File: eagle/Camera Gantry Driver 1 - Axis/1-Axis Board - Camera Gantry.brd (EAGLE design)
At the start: 73.3 x 46.5 mm, 48 parts, among them IC1 DRV8312A, U1 PTN78000, U2 DSPIC33FJ802GP-28, U3 LP2950-3.3ACZ

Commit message: Updating libraries and DRV83x2 related boards.
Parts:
- removed R6, R8, R9: (no value), pavlo:SMT-REF
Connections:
- removed net N$11: IC1.30, R8.1
- removed net N$12: IC1.38, R9.1
- removed net N$9: IC1.29, R6.1
- new net GND_A: IC1.29
- new net GND_B: IC1.30
- new net GND_C: IC1.38
- net GND: no longer R6.2, R8.2, R9.2
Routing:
- net N$12: track 21.8 -> 0.00 mm, vias 1 -> 0
- net N$9: track 10.4 -> 0.00 mm, vias 1 -> 0
- net N$11: track 9.39 -> 0.00 mm, vias 1 -> 0
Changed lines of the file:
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@@
 <?xml version="1.0" encoding="utf-8"?>
 <!DOCTYPE eagle SYSTEM "eagle.dtd">
-<eagle version="6.2">
+<eagle version="6.5.0">
 <drawing>
 <settings>
@@
 </class>
 </classes>
-<designrules>
+<designrules name="default">
 <description language="de">&lt;b&gt;EAGLE Design Rules&lt;/b&gt;
 &lt;p&gt;
@@
 <element name="E$3" library="ASL" package="STAND-OFF-TIGHT" value="" x="62.4" y="4"/>
 <element name="E$4" library="ASL" package="STAND-OFF-TIGHT" value="" x="11" y="4"/>
-<element name="R6" library="pavlo" package="SMT-REF" value="" x="18.364" y="30.75" rot="MR0"/>
-<element name="R8" library="pavlo" package="SMT-REF" value="" x="18.12" y="21.17" rot="MR90"/>
-<element name="R9" library="pavlo" package="SMT-REF" value="" x="26.38" y="14" rot="MR0"/>
 <element name="C18" library="ASL" package="CPOL-RADIAL-1000UF-25V" value="1000uF" x="23.622" y="35.96" rot="R270"/>
 <element name="C19" library="ASL" package="1206" value="10nF" x="21.082" y="42.672"/>
@@
 <wire x1="68.993" y1="11.23" x2="68.77" y2="11.23" width="0.4064" layer="1"/>
 <wire x1="68.77" y1="11.23" x2="67" y2="13" width="0.4064" layer="1"/>
-<contactref element="R6" pad="2"/>
-<contactref element="R8" pad="2"/>
-<contactref element="R9" pad="2"/>
 <contactref element="C19" pad="2"/>
 <contactref element="C18" pad="2"/>
@@
 <wire x1="31.5425" y1="22.8525" x2="32.25" y2="23.56" width="0.4064" layer="1"/>
 </signal>
-<signal name="N$9">
-<contactref element="IC1" pad="29"/>
-<contactref element="R6" pad="1"/>
-<wire x1="19.35" y1="26.0275" x2="17.4065" y2="26.0275" width="0.4064" layer="1"/>
-<wire x1="17.4065" y1="26.0275" x2="16.002" y2="27.432" width="0.4064" layer="1"/>
-<wire x1="16.002" y1="27.432" x2="14.986" y2="27.432" width="0.4064" layer="1"/>
-<wire x1="14.986" y1="27.432" x2="14.732" y2="27.178" width="0.4064" layer="1"/>
-<via x="14.732" y="27.178" extent="1-16" drill="0.6"/>
-<wire x1="14.732" y1="27.178" x2="14.732" y2="30.7756" width="0.4064" layer="16"/>
-<wire x1="14.732" y1="30.7756" x2="15.24" y2="30.7756" width="0.4064" layer="16"/>
-<wire x1="15.24" y1="30.7756" x2="16.2304" y2="30.75" width="0.4064" layer="16"/>
-</signal>
-<signal name="N$11">
-<contactref element="IC1" pad="30"/>
-<contactref element="R8" pad="1"/>
-<wire x1="19.35" y1="25.3925" x2="14.4855" y2="25.3925" width="0.4064" layer="1"/>
-<wire x1="14.4855" y1="25.3925" x2="14.478" y2="25.4" width="0.4064" layer="1"/>
-<via x="14.478" y="25.4" extent="1-16" drill="0.6"/>
-<wire x1="14.478" y1="25.4" x2="16.0236" y2="25.4" width="0.4064" layer="16"/>
-<wire x1="16.0236" y1="25.4" x2="18.12" y2="23.3036" width="0.4064" layer="16"/>
-</signal>
-<signal name="N$12">
-<contactref element="IC1" pad="38"/>
-<contactref element="R9" pad="1"/>
-<wire x1="19.35" y1="20.3125" x2="14.7245" y2="20.3125" width="0.4064" layer="1"/>
-<wire x1="14.7245" y1="20.3125" x2="14.478" y2="20.066" width="0.4064" layer="1"/>
-<via x="14.478" y="20.066" extent="1-16" drill="0.6"/>
-<wire x1="14.478" y1="20.066" x2="14.478" y2="14.224" width="0.4064" layer="16"/>
-<wire x1="14.478" y1="14.224" x2="16.002" y2="12.7" width="0.4064" layer="16"/>
-<wire x1="16.002" y1="12.7" x2="22.9464" y2="12.7" width="0.4064" layer="16"/>
-<wire x1="22.9464" y1="12.7" x2="24.2464" y2="14" width="0.4064" layer="16"/>
-</signal>
 <signal name="N$13">
 <contactref element="C19" pad="1"/>
@@
 <wire x1="17.78" y1="42.672" x2="19.682" y2="42.672" width="0.4064" layer="1"/>
 </signal>
+<signal name="GND_B">
+<contactref element="IC1" pad="30"/>
+</signal>
+<signal name="GND_A">
+<contactref element="IC1" pad="29"/>
+</signal>
+<signal name="GND_C">
+<contactref element="IC1" pad="38"/>
+</signal>
 </signals>

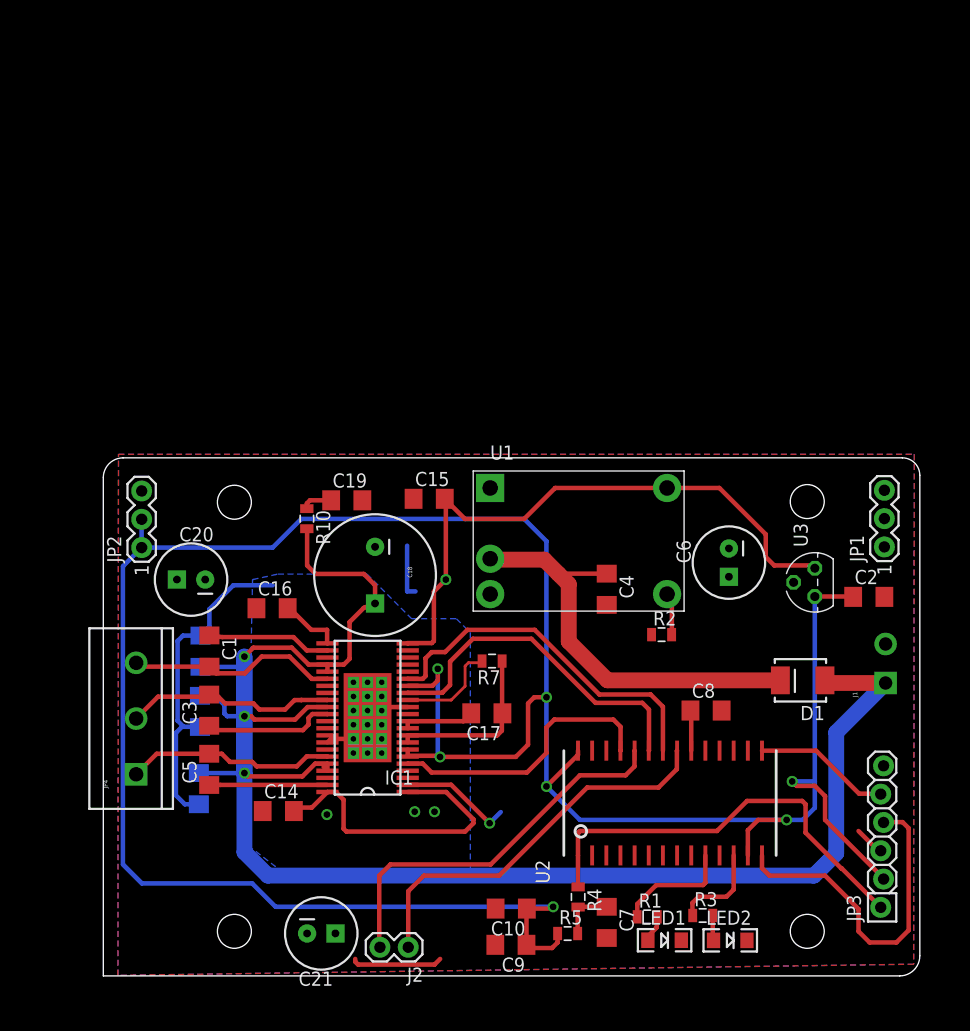
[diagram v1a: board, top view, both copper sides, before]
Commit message: More motor driver refactoring.
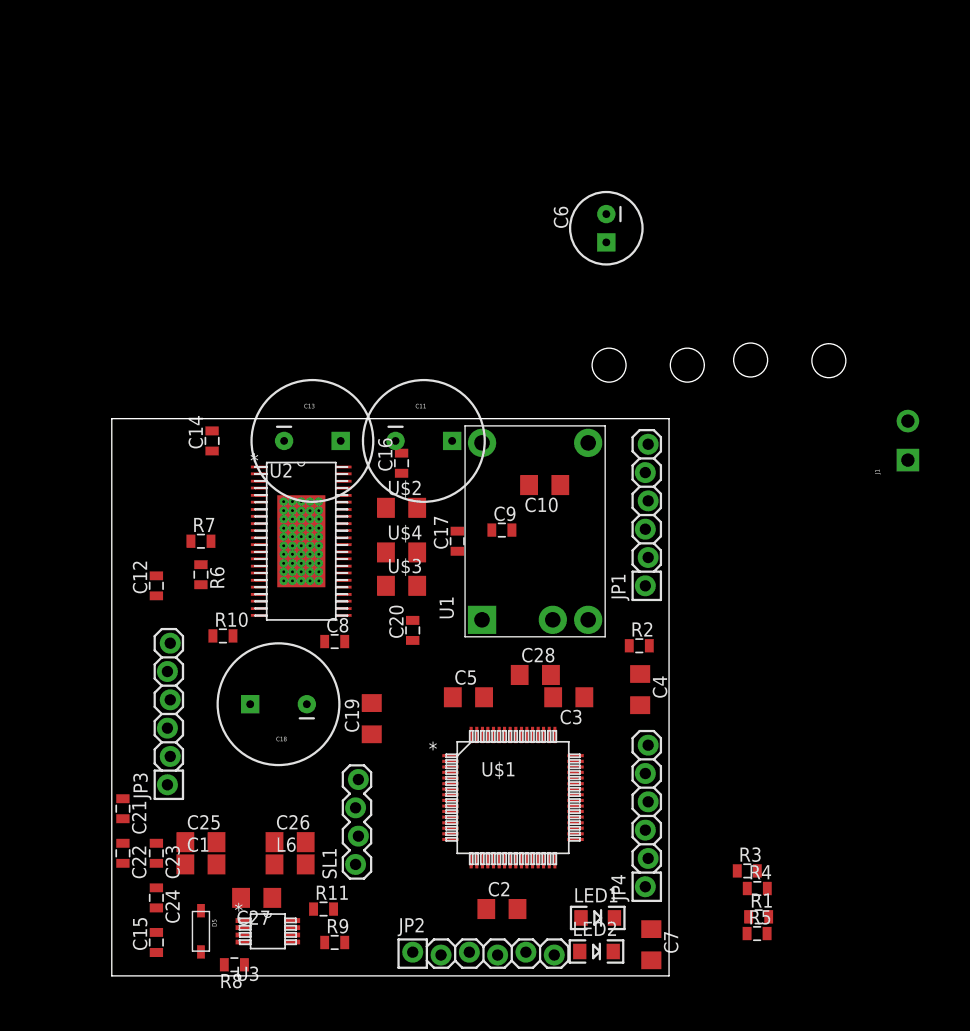
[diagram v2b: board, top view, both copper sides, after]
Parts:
- removed D1: DIODE-SCHOTTKY240A, CMPE118lib:SMA-DIODE-B240A
- removed IC1: DRV8312A, pavlo:TSSOP-44-POWERPAD
- removed J2: (no value), ASL:1X02
- added C22, C23: .1uF, ASL:0805
- added C24: 1.6nF, ASL:0805
- added C25: 10uF 16V, ASL:1206
- added C26: 1uF 16V, CMPE118lib:1206
- added C27: .1uF, CMPE118lib:1206
- added C28: 10uF, ASL:1206
- added D5: PMEG2010AEH, DRV83x2Support:SOD-123
- added L6: LQM31PN3R3M00L, DRV83x2Support:1206
- added R11: 158k, ASL:0805
- added R6: OC_ADJ, ASL:0805
- added R8: 47k, ASL:0805
- added R9: 18.2k, ASL:0805
- added SL1: (no value), ASL:1X04_LOCK
- added U$1: DSPIC33EP256MC506, DRV83x2Support:QFP64-10X10MC
- added U$2, U$3, U$4: ERJ-8BWJR010V, DRV83x2Support:1206
- C1, C3, C5: value 1uF -> .1uF; device ASL:1206 -> CMPE118lib:1206
- C11: value 100nF -> 330uF; device ASL:1206 -> ASL:CPOL-RADIAL-1000UF-25V
- C12: device ASL:1206 -> ASL:0805
- C13: value 100nF -> 47uF; device ASL:1206 -> ASL:CPOL-RADIAL-1000UF-25V
- C14, C15: value 220nF -> 1uF; device ASL:1206 -> ASL:0805
- C16: value 220nF -> .1uF; device ASL:1206 -> ASL:0805
- C17: value 100nF -> .1uF; device ASL:1206 -> ASL:0805
- C2: value 2.2uF -> .1uF; device ASL:1206 -> CMPE118lib:1206
- C20, C21: value 220uF -> .1uF; device ASL:CPOL-RADIAL-100UF-25V -> ASL:0805
- C8: value 10uF -> 1uF; device CMPE118lib:1206 -> ASL:0805
- C9: value .1uF -> 1uF; device CMPE118lib:1206 -> ASL:0805
- JP1, JP2: value M03PTH -> (none); device ASL:1X03 -> ASL:1X06_LOCK
- JP4: value M03-SCREW-5MM -> (none); device ASL:SCREWTERMINAL-5MM-3 -> ASL:1X06_LOCK
- R7: value 40~kOhm -> 1
- U2: value DSPIC33FJ802GP-28 -> DRV8312_DDW_44; device CMPE118lib:SOIC28-W -> DRV83x2Support:DDW44_8P26X4P31
- U3: value LP2950-3.3ACZ -> TPS61085_DGK_8; device ASL:TO92 -> DRV83x2Support:DGK8
- moved E$4 65.1 mm to (51.6, 54.8)
- moved JP3 64.9 mm to (5.12, 17.1)
- moved U3 58.2 mm to (14.0, 4.00), turned to 0 degrees
- moved E$1 54.8 mm to (64.3, 55.2)
- moved E$3 53.8 mm to (44.6, 54.8)
- moved JP4 46.9 mm to (48.0, 8.00)
- moved C15 46.7 mm to (4.00, 3.00), turned to 90 degrees
- moved JP2 45.9 mm to (27.0, 2.00), turned to 0 degrees
- moved C2 43.2 mm to (35.0, 6.00)
- moved U2 40.8 mm to (17.0, 39.0), turned to 0 degrees
- moved C10 38.1 mm to (38.8, 44.0)
- moved C9 37.2 mm to (35.0, 40.0), turned to 0 degrees
- moved C8 33.9 mm to (20.0, 30.0)
- moved C14 33.7 mm to (9.00, 48.0), turned to 90 degrees
- moved C3 32.3 mm to (41.0, 25.0), turned to 180 degrees
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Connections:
- removed net AGND: C17.1, IC1.8, IC1.9, R7.1
- removed net CAN_RX: U2.P$11
- removed net CAN_TX: U2.P$16
- removed net GND_A: IC1.29
- removed net GND_B: IC1.30
- removed net GND_C: IC1.38
- removed net N$18: C3.1, IC1.33
- removed net PWM1: IC1.5, U2.P$25
- removed net PWM2: IC1.15, U2.P$23
- removed net PWM3: IC1.17, U2.P$22
- removed net RA0: U2.P$2
- removed net RA2: U2.P$9
- removed net RB0: U2.P$4
- removed net RB1: U2.P$5
- removed net RB15: U2.P$26
- removed net RB2: U2.P$6
- removed net RB9: U2.P$18
- removed net TEMP: U2.P$3
- removed net UART_RX: J2.2, U2.P$24
- removed net UART_TX: J2.1, U2.P$21
- removed net VREG: C17.2, IC1.10, IC1.11
- removed net V_SENSE: U2.P$7
- new net FAULT: U$1.5, U2.18
- new net GVDD: C11.1, C13.1, C14.1, C15.1, C8.2, C9.2, D5.C, L6.2, R11.1, U2.1, U2.2, U2.22, U2.23, U2.44
- new net N$11: R8.1, U3.1
- new net N$12: C24.2, R8.2
- new net N$14: C28.1, U$1.56
- new net N$16: R11.2, R9.1, U3.2
- new net N$21: C16.2, U2.43
- new net N$22: JP2.6, U$1.44
- new net N$23: JP1.1, U$1.46
- new net N$24: JP1.2, U$1.49
- new net N$25: JP1.3, U$1.50
- new net N$27: JP1.5, U$1.52
- new net N$28: JP1.6, U$1.59
- new net N$29: JP2.2, U$1.6
- new net N$30: C17.2, U2.33
- new net N$32: JP1.4, U$1.51
- new net N$35: JP4.4, U$1.35
- new net N$36: JP4.5, U$1.36
- new net N$37: JP4.6, U$1.37
- new net N$38: JP4.3, U$1.34
- new net N$39: C20.1, U2.24
- new net N$40: SL1.1, U$1.15
- new net N$41: SL1.2, U$1.14
- new net N$42: SL1.3, U$1.13
- new net N$43: SL1.4, U$1.12
- new net N$44: JP4.2, U$1.33
- new net N$45: C12.2, R6.1, R7.1, U2.12, U2.8, U2.9
- new net N$47: C12.1, U2.10, U2.11
- new net N$9: C1.2, U$1.20
- new net OC_ADJ: R6.2, U2.14
- new net OTW: U$1.1, U2.21
- new net OUT_A: C20.2, U2.28
- new net OUT_B: C17.1, U2.31
- new net OUT_C: C16.1, U2.39
- new net PWM_A: U$1.2, U2.17
- new net PWM_B: U$1.62, U2.15
- new net PWM_C: U$1.60, U2.5
- new net RESET_A: U$1.3, U2.16
- new net RESET_B: U$1.63, U2.7
- new net RESET_C: U$1.61, U2.6
- net GND: now also C10.1, C14.2, C15.2, C2.1, C22.2, C23.2, C24.1, C25.1, C26.2, C27.2, C28.2, C3.1, C5.2, C8.1, C9.1, JP4.1, R7.2, R9.2, U$1.25, U$1.41, U$1.9, U$2.2, U$3.2, U$4.2, U2.13, U2.36, U2.37, U2.EPAD, U3.4; no longer C10.2, C12.2, C14.1, C15.1, C16.1, C2.2, C20.2, C8.2, C9.2, IC1.12, IC1.13, IC1.36, IC1.37, IC1.45, IC1.46, IC1.47, IC1.48, IC1.49, IC1.50, IC1.51, IC1.52, IC1.53, IC1.54, IC1.55, IC1.56, IC1.57, IC1.58, IC1.59, IC1.60, IC1.61, IC1.62, IC1.63, JP1.3, U2.P$19, U2.P$27, U2.P$8, U3.2
- net LED1: now also U$1.22; no longer U2.P$10
- net LED2: now also U$1.23; no longer U2.P$12
- net MCLR: now also U$1.7; no longer U2.P$1
- net N$10: now also C27.1, U3.8; no longer C5.2, IC1.39, JP4.1
- net N$15: now also D5.A, U3.5; no longer U2.P$17
- net N$17: now also JP2.1, U$1.4; no longer C1.1, IC1.24
- net N$19: now also JP2.4, U$1.32; no longer C5.1, IC1.43
- net N$20: now also JP2.5, U$1.43; no longer IC1.14, R7.2
- net N$4: now also U$2.1, U2.38; no longer C1.2, IC1.28, JP4.3
- net N$5: now also U$3.1, U2.29; no longer C3.2, IC1.31, JP4.2
- net N$7: now also U$4.1, U2.30; no longer C8.1, U2.P$20
- net N$8: now also C1.1, U$1.19; no longer C4.1, D1.C, U1.V_IN
- net PGC: now also U$1.17; no longer U2.P$15
- net PGD: now also U$1.18; no longer U2.P$14
- net PVDD: now also C21.1, C22.1, C23.1, C4.1, U1.V_IN, U2.26, U2.27, U2.32, U2.40, U2.41; no longer C11.1, C12.1, C13.1, D1.A, IC1.26, IC1.27, IC1.32, IC1.40, IC1.41
- net VCC: now also C10.2, C2.2, C25.2, C26.1, C3.2, C5.1, L6.1, U$1.10, U$1.26, U$1.38, U$1.57, U3.6, U3.7; no longer C14.2, C15.2, C16.2, C20.1, C21.1, IC1.1, IC1.2, IC1.22, IC1.23, IC1.44, JP1.1, JP1.2
- net VCC3V3: no longer C10.1, C2.1, C9.1, IC1.16, IC1.6, IC1.7, JP2.1, JP2.2, U2.P$13, U2.P$28, U3.1
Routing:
- net VCC3V3: track 244.9 -> 0.00 mm, vias 7 -> 0
- net PVDD: track 165.4 -> 0.00 mm, vias 3 -> 0
- net VCC: track 103.1 -> 0.00 mm, vias 2 -> 0
- net GND: track 46.3 -> 0.00 mm, vias 3 -> 0
- net MCLR: track 38.7 -> 0.00 mm
- net N$8: track 37.9 -> 0.00 mm
- net UART_TX: track 35.3 -> 0.00 mm
- net UART_RX: track 34.8 -> 0.00 mm
- net PWM3: track 32.5 -> 0.00 mm
- net PWM2: track 31.2 -> 0.00 mm
- net PGD: track 30.3 -> 0.00 mm
- net PWM1: track 25.2 -> 0.00 mm
- net N$5: track 19.6 -> 0.00 mm
- net N$4: track 19.0 -> 0.00 mm
- net N$10: track 18.8 -> 0.00 mm
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- removed copper zone on layer 1, net GND
- removed copper zone on layer 16, net GND
- removed copper zone on layer 16, net VCC
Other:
- board size 73.3 x 46.5 mm -> 50 x 50 mm

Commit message: More work on the new driver boards.
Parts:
- added JP5: M03SCREW_LOCK, ASL:SCREWTERMINAL-3.5MM-3_LOCK.007S
- C1, C10, C2, C26, C27, C3, C5, C7: device CMPE118lib:1206 -> ASL:0805
- C19: device ASL:1206 -> ASL:0805
- moved E$3 65.4 mm to (3.62, 3.80)
- moved C18 64.2 mm to (47.0, 80.0)
- moved JP3 61.1 mm to (64.3, 2.00), turned to 180 degrees
- moved E$2 52.6 mm to (70.3, 4.26)
- moved E$4 50.3 mm to (3.64, 39.8)
- moved C25 47.7 mm to (48.0, 38.0)
- moved R8 44.9 mm to (35.0, 39.0), turned to 270 degrees
- moved R5 43.7 mm to (14.9, 11.8)
- moved R4 43.0 mm to (14.9, 9.84)
- moved C24 40.6 mm to (29.0, 39.0)
- moved D5 38.2 mm to (34.0, 32.0)
- moved C23 36.2 mm to (27.0, 39.0), turned to 90 degrees
- moved C26 35.5 mm to (39.0, 39.0), turned to 270 degrees
- moved JP1 33.1 mm to (64.0, 6.00)
- moved R11 33.0 mm to (36.7, 33.9)
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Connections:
- net OUT_A: now also JP5.3
- net OUT_B: now also JP5.2
- net OUT_C: now also JP5.1
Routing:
- net N$16: track 0.00 -> 20.4 mm
- net VCC: track 0.00 -> 17.1 mm
- net OUT_C: track 0.00 -> 14.5 mm, vias 0 -> 2
- net OUT_A: track 0.00 -> 14.5 mm, vias 0 -> 2
- net OUT_B: track 0.00 -> 14.3 mm, vias 0 -> 2
- net PVDD: track 0.00 -> 13.4 mm
- net GVDD: track 0.00 -> 8.40 mm
- net N$47: track 0.00 -> 4.89 mm
- net N$45: track 0.00 -> 4.89 mm
- net N$5: track 0.00 -> 4.43 mm
- net N$7: track 0.00 -> 4.42 mm
- net N$4: track 0.00 -> 4.13 mm
- net N$30: track 0.00 -> 3.15 mm
- net N$21: track 0.00 -> 2.43 mm
- net N$39: track 0.00 -> 2.33 mm
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- added copper zone on layer 1, net GND
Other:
- board size 50 x 50 mm -> 75 x 44 mm

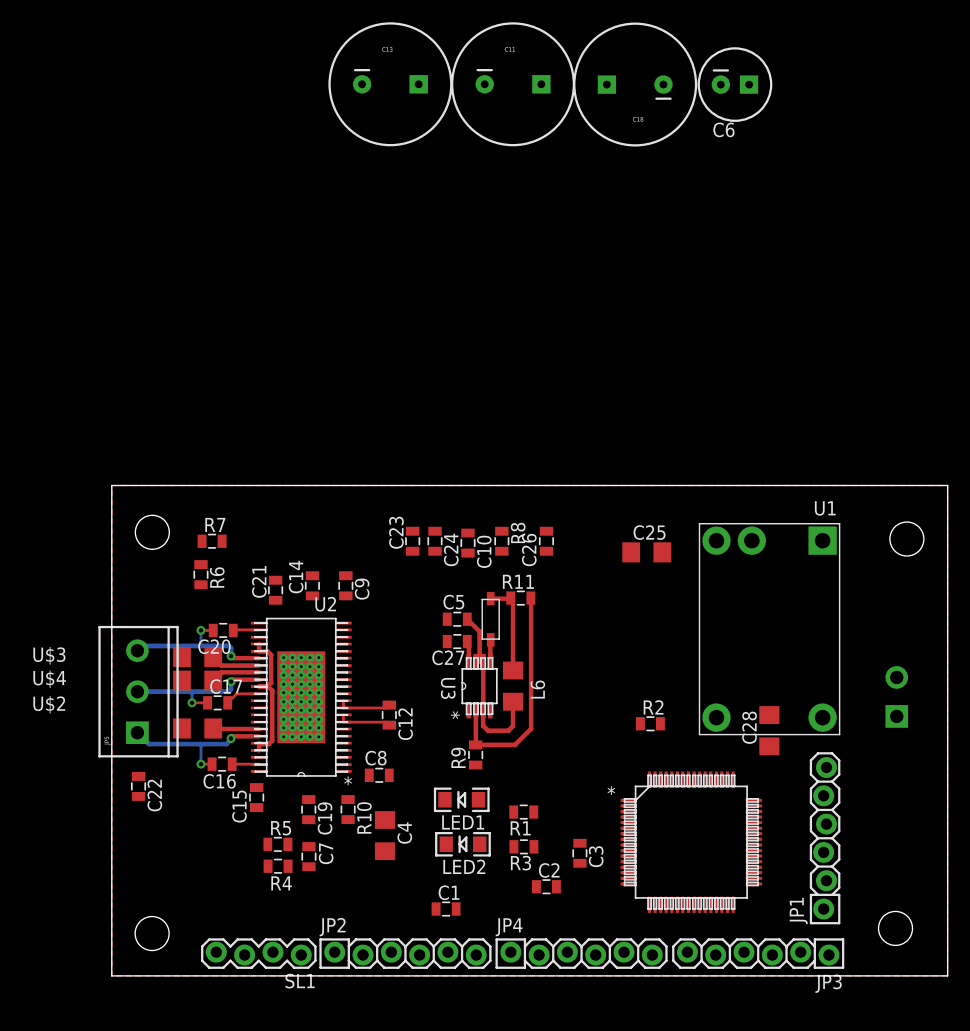
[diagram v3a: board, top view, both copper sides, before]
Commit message: Did some clean-up to the directory, added an ams EasyPoint breakout board and consolidated PMSMmini board as well as pavlo.lbr.
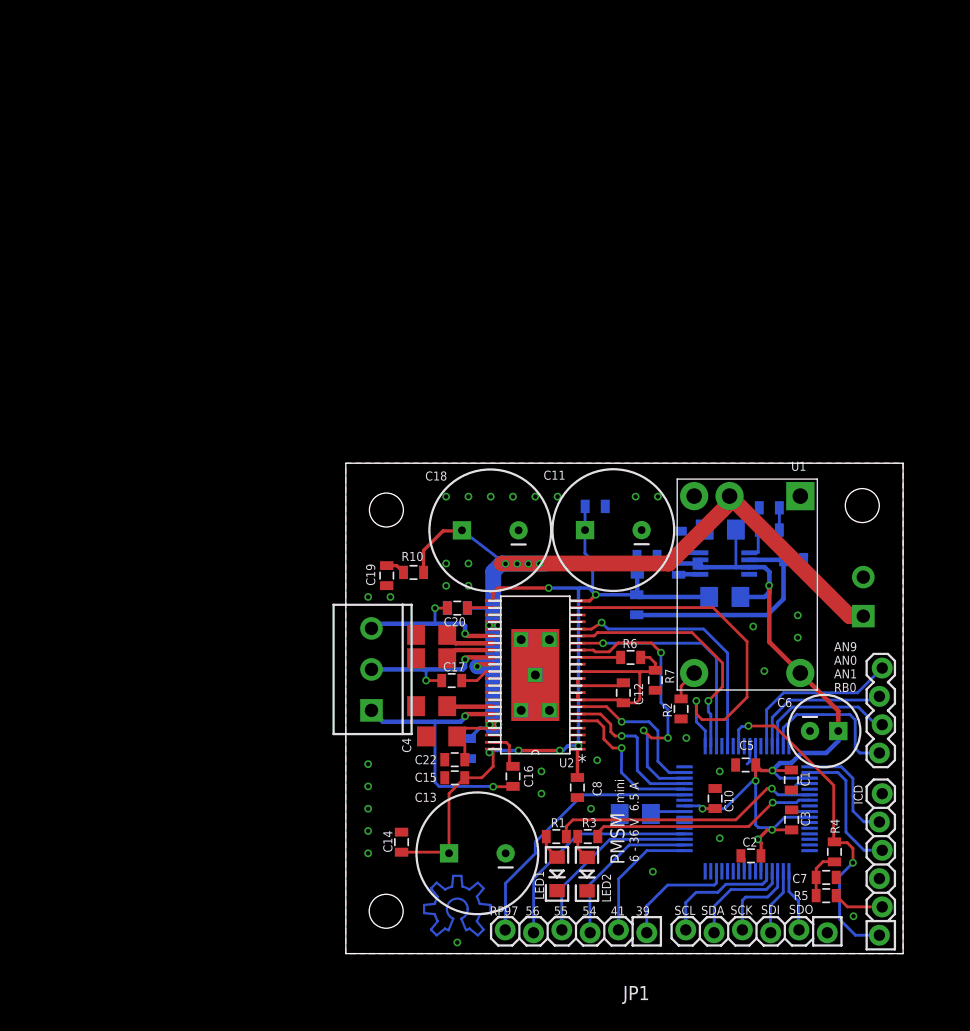
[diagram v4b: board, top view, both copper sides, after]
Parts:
- removed E$2: (no value), ASL:STAND-OFF-TIGHT
- removed JP2: (no value), ASL:1X06_LOCK
- moved C13 69.4 mm to (32.8, 11.0), turned to 180 degrees
- moved C6 58.5 mm to (63.9, 22.0)
- moved SL1 55.0 mm to (69.0, 20.0), turned to 90 degrees
- moved R4 49.9 mm to (64.8, 11.1), turned to 270 degrees
- moved R5 49.4 mm to (64.1, 7.20), turned to 180 degrees
- moved C7 46.4 mm to (64.1, 8.84), turned to 0 degrees
- moved C18 42.1 mm to (34.0, 40.0)
- moved R7 41.7 mm to (48.8, 26.5), turned to 270 degrees
- moved C11 41.0 mm to (45.0, 40.0), turned to 180 degrees
- moved R6 39.3 mm to (46.5, 28.6), turned to 180 degrees
- moved R9 33.5 mm to (61.2, 37.4), flipped to the bottom, turned to 180 degrees
- moved C1 33.1 mm to (61.0, 17.6), turned to 270 degrees
- moved C10 31.9 mm to (54.1, 15.9)
- moved C24 30.1 mm to (59.0, 42.0), flipped to the bottom, turned to 180 degrees
- moved C5 29.0 mm to (56.9, 18.9)
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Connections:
- removed net N$17: JP2.1, U$1.4
- removed net N$19: JP2.4, U$1.32
- removed net N$20: JP2.5, U$1.43
- removed net N$22: JP2.6, U$1.44
- removed net N$29: JP2.2, U$1.6
- removed net N$8: C1.1, U$1.19
- removed net N$9: C1.2, U$1.20
- net GND: now also C1.2, U$1.20, U2.P$1, U2.P$2, U2.P$3, U2.P$7, U2.P$8; no longer JP2.3
- net VCC: now also C1.1, U$1.19
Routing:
- net PVDD: track 13.4 -> 87.1 mm, vias 0 -> 9
- net GVDD: track 8.40 -> 75.9 mm, vias 0 -> 6
- net VCC: track 17.1 -> 82.3 mm, vias 0 -> 6
- net OTW: track 0.00 -> 32.6 mm, vias 0 -> 1
- net MCLR: track 0.00 -> 30.4 mm, vias 0 -> 2
- net N$8: track 0.00 -> 28.4 mm
- net PWM_B: track 0.00 -> 25.8 mm, vias 0 -> 3
- net LED1: track 0.00 -> 24.4 mm, vias 0 -> 1
- net N$28: track 0.00 -> 24.1 mm
- net FAULT: track 0.00 -> 23.1 mm, vias 0 -> 1
- net PWM_A: track 0.00 -> 22.3 mm, vias 0 -> 1
- net RESET_A: track 0.00 -> 20.9 mm, vias 0 -> 1
- net LED2: track 0.00 -> 20.6 mm, vias 0 -> 1
- net N$27: track 0.00 -> 20.1 mm
- net N$32: track 0.00 -> 16.6 mm
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- added copper zone on layer 16, net GND
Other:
- board size 75 x 44 mm -> 50 x 44 mm
- board text added: "(C) - Pavlo Manovi 2013"
- board text added: "6 - 36 V 6.5 A"
- board text added: "AN9 AN0 AN1 RB0"
- board text added: "ICD"
- board text added: "PMSM"
- board text added: "RP97 56 55 54 41 39"
- board text added: "Released Under The TAPR OHL"
- board text added: "SCK"
- board text added: "SCL"
- board text added: "SDA"
- board text added: "SDI"
- board text added: "SDO"
- board text added: "mini"
